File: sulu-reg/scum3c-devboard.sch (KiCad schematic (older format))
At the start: 36 parts, among them J1 Conn_02x11_Odd_Even, J2 Conn_02x10_Odd_Even, J3 Conn_01x10, J4 73391-0060, U2 S-85S1AB18-I6T1U, U3 S-85S1AB11-I6T1U, U9AB1 ICM-20948

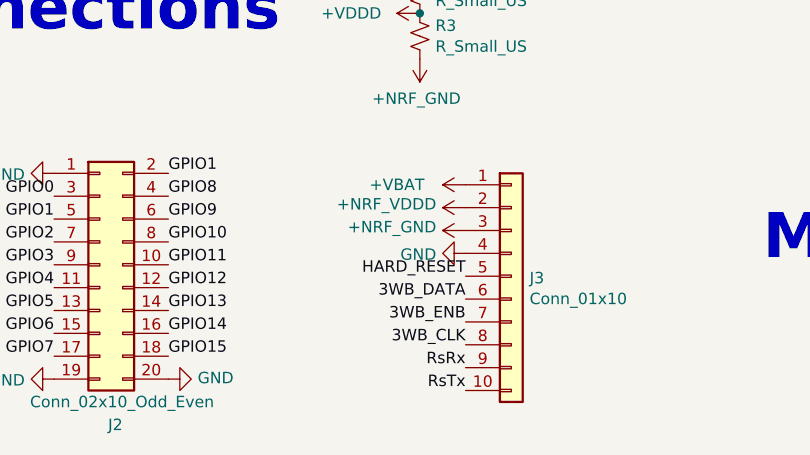
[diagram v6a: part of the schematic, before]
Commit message: flipped around the nrf header
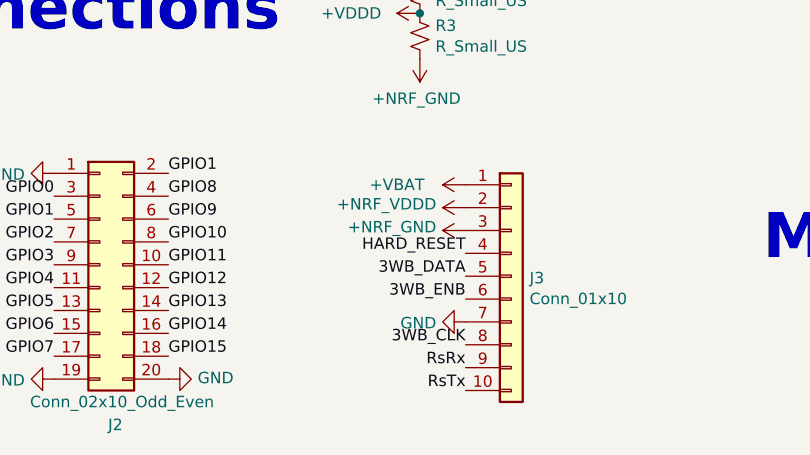
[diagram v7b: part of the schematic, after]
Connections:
- net 3WB_DATA: now also J3.5 (Pin_5); no longer J3.6 (Pin_6)
- net 3WB_ENB: now also J3.6 (Pin_6); no longer J3.7 (Pin_7)
- net GND: now also J3.7 (Pin_7); no longer J3.4 (Pin_4)
- net HARD_RESET: now also J3.4 (Pin_4); no longer J3.5 (Pin_5)
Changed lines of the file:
@@
 L power:GND #PWR021
 U 1 1 607605CB
-P 5100 7150
-F 0 "#PWR021" H 5100 6900 50  0001 C CNN
-F 1 "GND" V 5105 7022 50  0000 R CNN
-F 2 "" H 5100 7150 50  0001 C CNN
-F 3 "" H 5100 7150 50  0001 C CNN
-	1    5100 7150
+P 5100 7450
+F 0 "#PWR021" H 5100 7200 50  0001 C CNN
+F 1 "GND" V 5105 7322 50  0000 R CNN
+F 2 "" H 5100 7450 50  0001 C CNN
+F 3 "" H 5100 7450 50  0001 C CNN
+	1    5100 7450
 	0    1    1    0
 $EndComp
+Text Label 5100 7250 2    50   ~ 0
+3WB_DATA
 Text Label 5100 7350 2    50   ~ 0
-3WB_DATA
-Text Label 5100 7450 2    50   ~ 0
 3WB_ENB
 Text Label 5100 7550 2    50   ~ 0
 3WB_CLK
-Text Label 5100 7250 2    50   ~ 0
+Text Label 5100 7150 2    50   ~ 0
 HARD_RESET
 $Comp
